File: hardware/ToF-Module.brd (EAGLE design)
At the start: 23 x 18 mm, 25 parts, among them CON1 JST-03, CON2 JST-03, U1 ATMEGA328P, U2 BSS138DWQ, U3 MIC5504_2.8YM5, X1 RESONATOR8M00

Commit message: PCB: first version
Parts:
- removed R1, R2, R3, R4, R5, R6, R7: 10k, resistor:R0603
- removed TP1, TP2, TP3, TP4: PTR1TP20SQ, testpad:TP20SQ
- added EN, IRQ, SCL, SDA: PTR1TP20SQ, testpad:TP20SQ
- added RN1, RN2: 10k, resistor-dil:CAT16
- C1, C2: value 1µF -> 4.7µF
- C5: value 4.7µF -> 0.1µF
- C6: value 0.1µF -> 10µF; device resistor:C0603 -> resistor:C0805
- moved C6 15.5 mm to (14.0, 4.50)
- moved C1 13.0 mm to (13.5, 15.0), turned to 90 degrees
- moved X1 11.5 mm to (21.0, 3.50), turned to 90 degrees
- moved C5 11.1 mm to (18.0, 4.50), turned to 180 degrees
- moved C2 11.0 mm to (16.5, 12.0)
- moved C3 6.59 mm to (20.5, 15.1), turned to 180 degrees
- moved C4 6.58 mm to (20.5, 13.0), turned to 180 degrees
- moved U2 5.70 mm to (13.5, 7.50), turned to 180 degrees
- moved U3 2.69 mm to (16.5, 15.0), turned to 270 degrees
- moved VL1 2.00 mm to (21.0, 9.00), turned to 90 degrees
- moved CON1 0.20 mm to (2.80, 5.00)
- moved CON2 0.20 mm to (2.80, 13.0)
- moved JP1 0.10 mm to (8.90, 9.00)
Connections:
- net +2V8: now also RN1.5, RN1.6, RN1.7, RN1.8; no longer R1.2, R2.2, R3.2, R4.2
- net EXT_IRQ: now also IRQ.TP; no longer TP4.TP
- net EXT_XSHUT: now also EN.TP; no longer TP3.TP
- net IRQ: now also RN1.4; no longer R4.1
- net N$3: now also RN1.2; no longer R1.1
- net N$4: now also RN1.1; no longer R2.1
- net RESET: now also RN2.3; no longer R7.2
- net SCL: now also RN2.1, SCL.TP; no longer R6.1, TP2.TP
- net SDA: now also RN2.2, SDA.TP; no longer R5.1, TP1.TP
- net VIN: now also RN2.6, RN2.7, RN2.8; no longer R5.2, R6.2, R7.1
- net XSHUT: now also RN1.3; no longer R3.1
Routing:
- net VIN: track 0.00 -> 66.8 mm, vias 0 -> 2
- net SCL: track 0.00 -> 28.1 mm, vias 0 -> 2
- net DATA: track 0.00 -> 25.7 mm
- net SDA: track 0.00 -> 22.3 mm, vias 0 -> 2
- net +2V8: track 0.00 -> 22.1 mm
- net EXT_IRQ: track 0.00 -> 21.8 mm, vias 0 -> 1
- net EXT_XSHUT: track 0.00 -> 18.7 mm, vias 0 -> 1
- net RESET: track 0.00 -> 16.4 mm, vias 0 -> 1
- net N$3: track 0.00 -> 14.4 mm
- net XSHUT: track 0.00 -> 14.2 mm, vias 0 -> 2
- net MISO: track 0.00 -> 12.7 mm
- net IRQ: track 0.00 -> 9.43 mm, vias 0 -> 2
- net SCK: track 0.00 -> 9.06 mm
- net MOSI: track 0.00 -> 8.92 mm
- net N$4: track 0.00 -> 7.82 mm
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- added copper zone on layer 1, net GND
- added copper zone on layer 16, net GND
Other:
- board text added: "GobGob Senpai v1 08-2019"

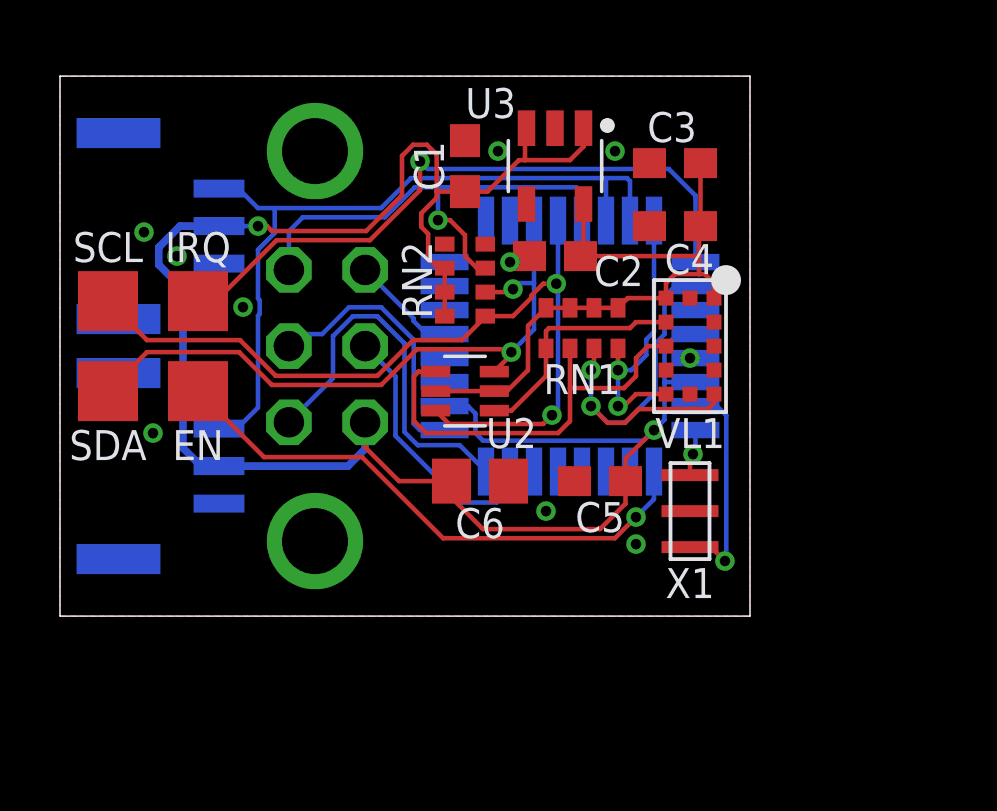
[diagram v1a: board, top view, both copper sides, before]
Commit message: hardware: add pullup for ext IRQ line + debug pads
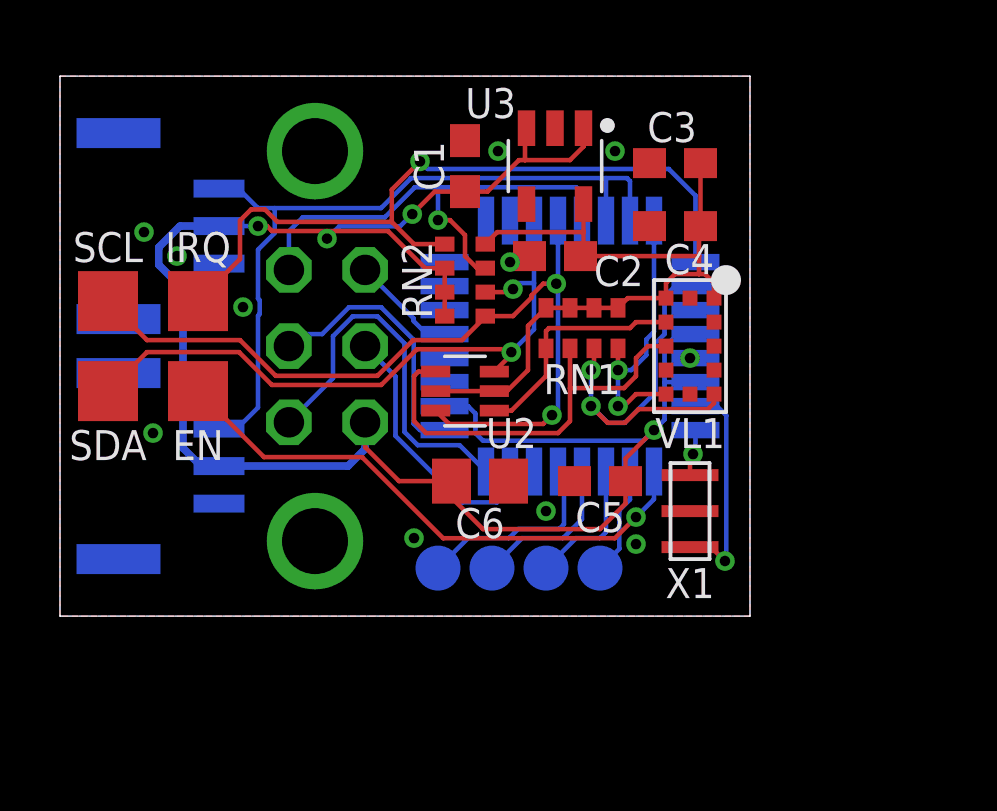
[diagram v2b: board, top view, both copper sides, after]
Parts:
- added DEBUG_A, DEBUG_B, DEBUG_C, DEBUG_D: PTR1TP15R, testpad:TP15R
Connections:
- new net N$1: DEBUG_A.TP, U1.10
- new net N$2: DEBUG_B.TP, U1.11
- new net N$7: DEBUG_C.TP, U1.12
- new net N$8: DEBUG_D.TP, U1.13
- net +2V8: now also RN2.4
- net EXT_IRQ: now also RN2.5
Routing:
- net N$8: track 0.00 -> 6.65 mm
- net N$7: track 0.00 -> 5.26 mm
- net N$2: track 0.00 -> 4.52 mm
- net N$1: track 0.00 -> 3.63 mm
- net +2V8: track 22.1 -> 25.6 mm
- net EXT_IRQ: track 21.8 -> 25.0 mm
- net VIN: track 66.8 -> 65.5 mm, vias 2 -> 4
- net GND: track 3.59 -> 4.32 mm, vias 12 -> 13
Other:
- board text added: "A"
- board text added: "B"
- board text added: "C"
- board text added: "D"
